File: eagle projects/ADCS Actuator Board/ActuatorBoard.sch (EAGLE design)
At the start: 142 parts, among them J19 TE_1-84953-1, J20 TE_1-84953-1, J21 TE_1-84953-1, U1 TVS991, U10 DRV10970_MOTOR_DRIVERDRV10970, U12 DRV10970_MOTOR_DRIVERDRV10970, U2 ADS7841E_2K5, U3 ADS7841E_2K5, U35 BD6210F-E2, U39 BD6210F-E2, U5 TVS991, U7 DRV10970_MOTOR_DRIVERDRV10970, U8 TVS991, U9 BD6210F-E2

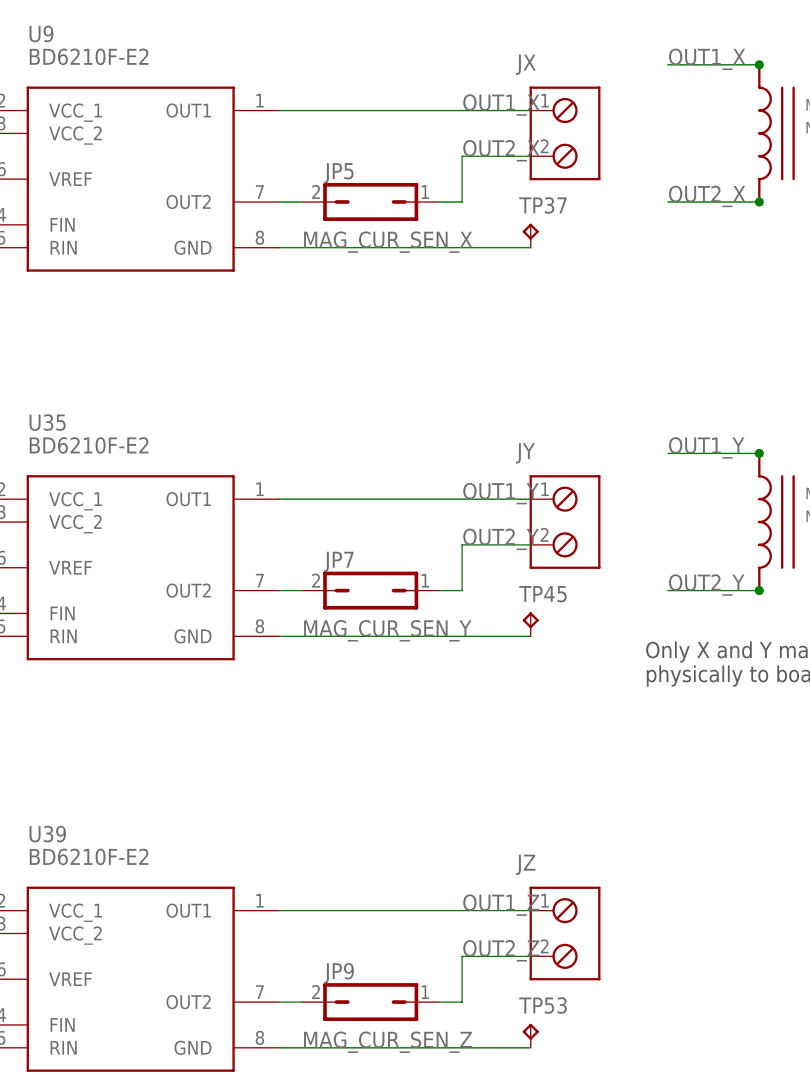
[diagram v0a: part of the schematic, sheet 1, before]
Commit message: Schematic Updates
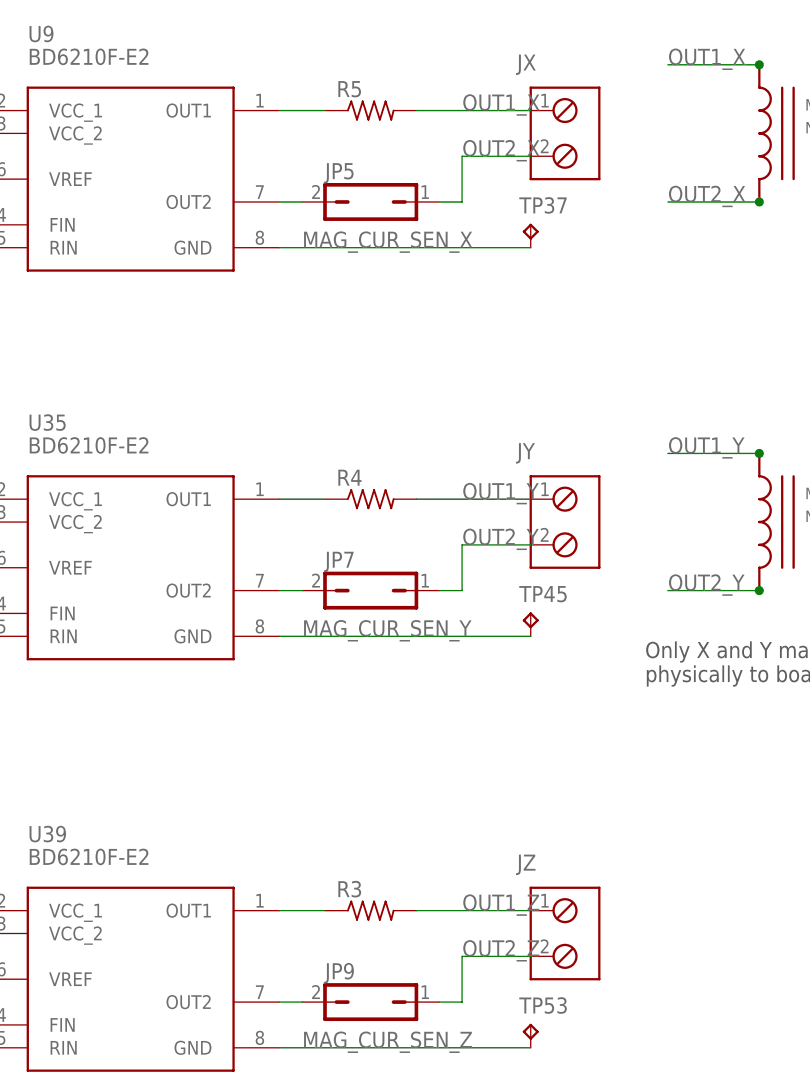
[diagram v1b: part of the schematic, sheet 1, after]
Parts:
- added R3, R4, R5: (no value), rcl:R-US_M0805
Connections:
- new net N$1: R3.1, U39.OUT1
- new net N$2: R4.1, U35.OUT1
- new net N$3: R5.1, U9.OUT1
- net OUT1_X: now also R5.2; no longer U9.OUT1
- net OUT1_Y: now also R4.2; no longer U35.OUT1
- net OUT1_Z: now also R3.2; no longer U39.OUT1
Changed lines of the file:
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@@
 <part name="R12" library="rcl" library_urn="urn:adsk.eagle:library:334" deviceset="R-US_" device="R0402" package3d_urn="urn:adsk.eagle:package:23547/3" value="4.7k"/>
 <part name="R15" library="rcl" library_urn="urn:adsk.eagle:library:334" deviceset="R-US_" device="R0402" package3d_urn="urn:adsk.eagle:package:23547/3" value="4.7k"/>
+<part name="R3" library="rcl" library_urn="urn:adsk.eagle:library:334" deviceset="R-US_" device="M0805" package3d_urn="urn:adsk.eagle:package:23556/2"/>
+<part name="R4" library="rcl" library_urn="urn:adsk.eagle:library:334" deviceset="R-US_" device="M0805" package3d_urn="urn:adsk.eagle:package:23556/2"/>
+<part name="R5" library="rcl" library_urn="urn:adsk.eagle:library:334" deviceset="R-US_" device="M0805" package3d_urn="urn:adsk.eagle:package:23556/2"/>
 </parts>
 <sheets>
@@
 <attribute name="VALUE" x="227.33" y="148.59" size="1.27" layer="96"/>
 </instance>
+<instance part="R3" gate="G$1" x="96.52" y="106.68" smashed="yes">
+<attribute name="NAME" x="92.71" y="108.1786" size="1.778" layer="95"/>
+<attribute name="VALUE" x="92.71" y="103.378" size="1.778" layer="96"/>
+</instance>
+<instance part="R4" gate="G$1" x="96.52" y="152.4" smashed="yes">
+<attribute name="NAME" x="92.71" y="153.8986" size="1.778" layer="95"/>
+<attribute name="VALUE" x="92.71" y="149.098" size="1.778" layer="96"/>
+</instance>
+<instance part="R5" gate="G$1" x="96.52" y="195.58" smashed="yes">
+<attribute name="NAME" x="92.71" y="197.0786" size="1.778" layer="95"/>
+<attribute name="VALUE" x="92.71" y="192.278" size="1.778" layer="96"/>
+</instance>
 </instances>
 <busses>
@@
 </segment>
 <segment>
-<pinref part="U9" gate="G$1" pin="OUT1"/>
 <pinref part="JX" gate="G$1" pin="1"/>
-<wire x1="114.3" y1="195.58" x2="86.36" y2="195.58" width="0.1524" layer="91"/>
 <label x="106.68" y="195.58" size="1.778" layer="95"/>
+<wire x1="114.3" y1="195.58" x2="101.6" y2="195.58" width="0.1524" layer="91"/>
+<pinref part="R5" gate="G$1" pin="2"/>
 </segment>
 </net>
@@
 </segment>
 <segment>
-<pinref part="U35" gate="G$1" pin="OUT1"/>
 <pinref part="JY" gate="G$1" pin="1"/>
-<wire x1="114.3" y1="152.4" x2="86.36" y2="152.4" width="0.1524" layer="91"/>
 <label x="106.68" y="152.4" size="1.778" layer="95"/>
+<wire x1="114.3" y1="152.4" x2="101.6" y2="152.4" width="0.1524" layer="91"/>
+<pinref part="R4" gate="G$1" pin="2"/>
 </segment>
 </net>
 <net name="OUT1_Z" class="0">
 <segment>
-<pinref part="U39" gate="G$1" pin="OUT1"/>
 <pinref part="JZ" gate="G$1" pin="1"/>
-<wire x1="114.3" y1="106.68" x2="86.36" y2="106.68" width="0.1524" layer="91"/>
 <label x="106.68" y="106.68" size="1.778" layer="95"/>
+<wire x1="114.3" y1="106.68" x2="101.6" y2="106.68" width="0.1524" layer="91"/>
+<pinref part="R3" gate="G$1" pin="2"/>
 </segment>
 </net>
@@
 <pinref part="U35" gate="G$1" pin="GND"/>
 <label x="88.9" y="137.16" size="1.778" layer="95"/>
+</segment>
+</net>
+<net name="N$1" class="0">
+<segment>
+<pinref part="U39" gate="G$1" pin="OUT1"/>
+<wire x1="91.44" y1="106.68" x2="86.36" y2="106.68" width="0.1524" layer="91"/>
+<pinref part="R3" gate="G$1" pin="1"/>
+</segment>
+</net>
+<net name="N$2" class="0">
+<segment>
+<pinref part="U35" gate="G$1" pin="OUT1"/>
+<wire x1="91.44" y1="152.4" x2="86.36" y2="152.4" width="0.1524" layer="91"/>
+<pinref part="R4" gate="G$1" pin="1"/>
+</segment>
+</net>
+<net name="N$3" class="0">
+<segment>
+<pinref part="U9" gate="G$1" pin="OUT1"/>
+<wire x1="91.44" y1="195.58" x2="86.36" y2="195.58" width="0.1524" layer="91"/>
+<pinref part="R5" gate="G$1" pin="1"/>
 </segment>
 </net>
@@
 <text x="111.76" y="53.34" size="1.778" layer="97">NC</text>
 <text x="261.62" y="7.62" size="2.54" layer="94">A</text>
-<text x="182.88" y="53.34" size="1.778" layer="97">Hall sensors on Maxon motor require external pull-up resistor</text>
+<text x="175.26" y="208.28" size="1.778" layer="97">Hall sensors on Maxon motor require external pull-up resistor</text>
 <text x="68.58" y="200.66" size="1.778" layer="97">Only Z-axis Reaction wheel mounted physically to PCB</text>
 </plain>

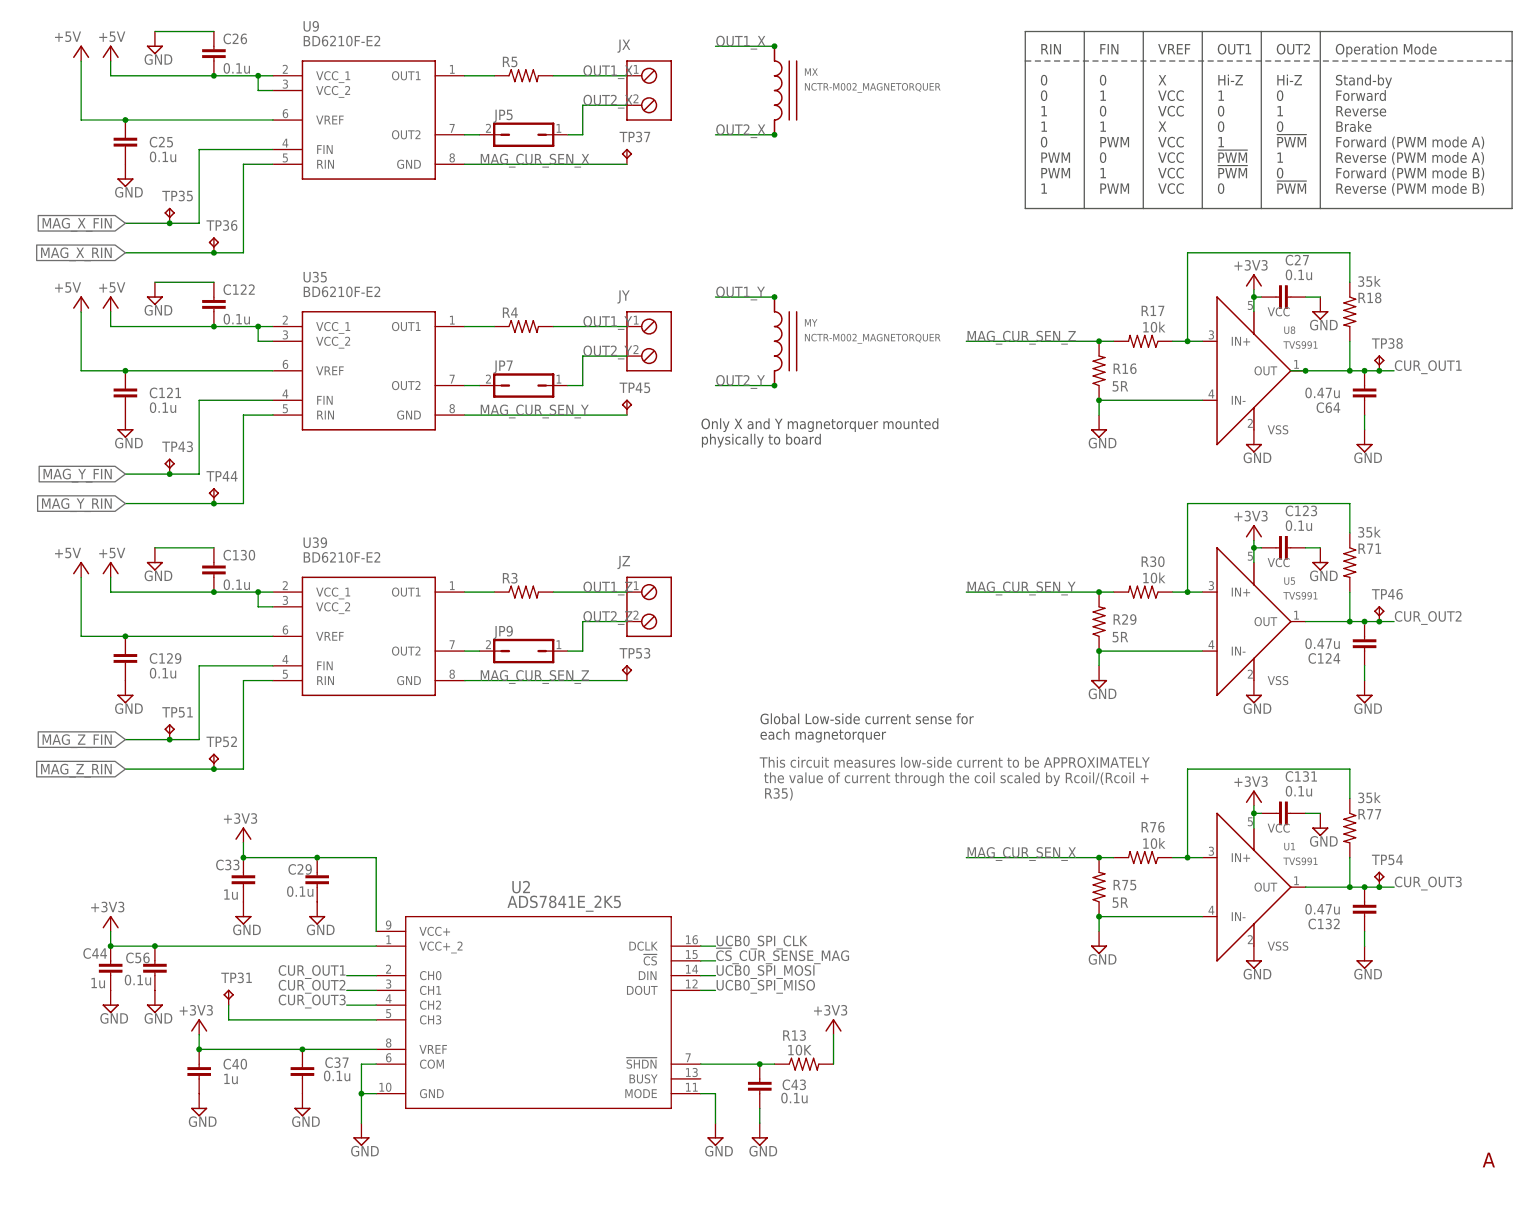
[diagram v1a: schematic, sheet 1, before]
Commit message: Updated current sense circuitry
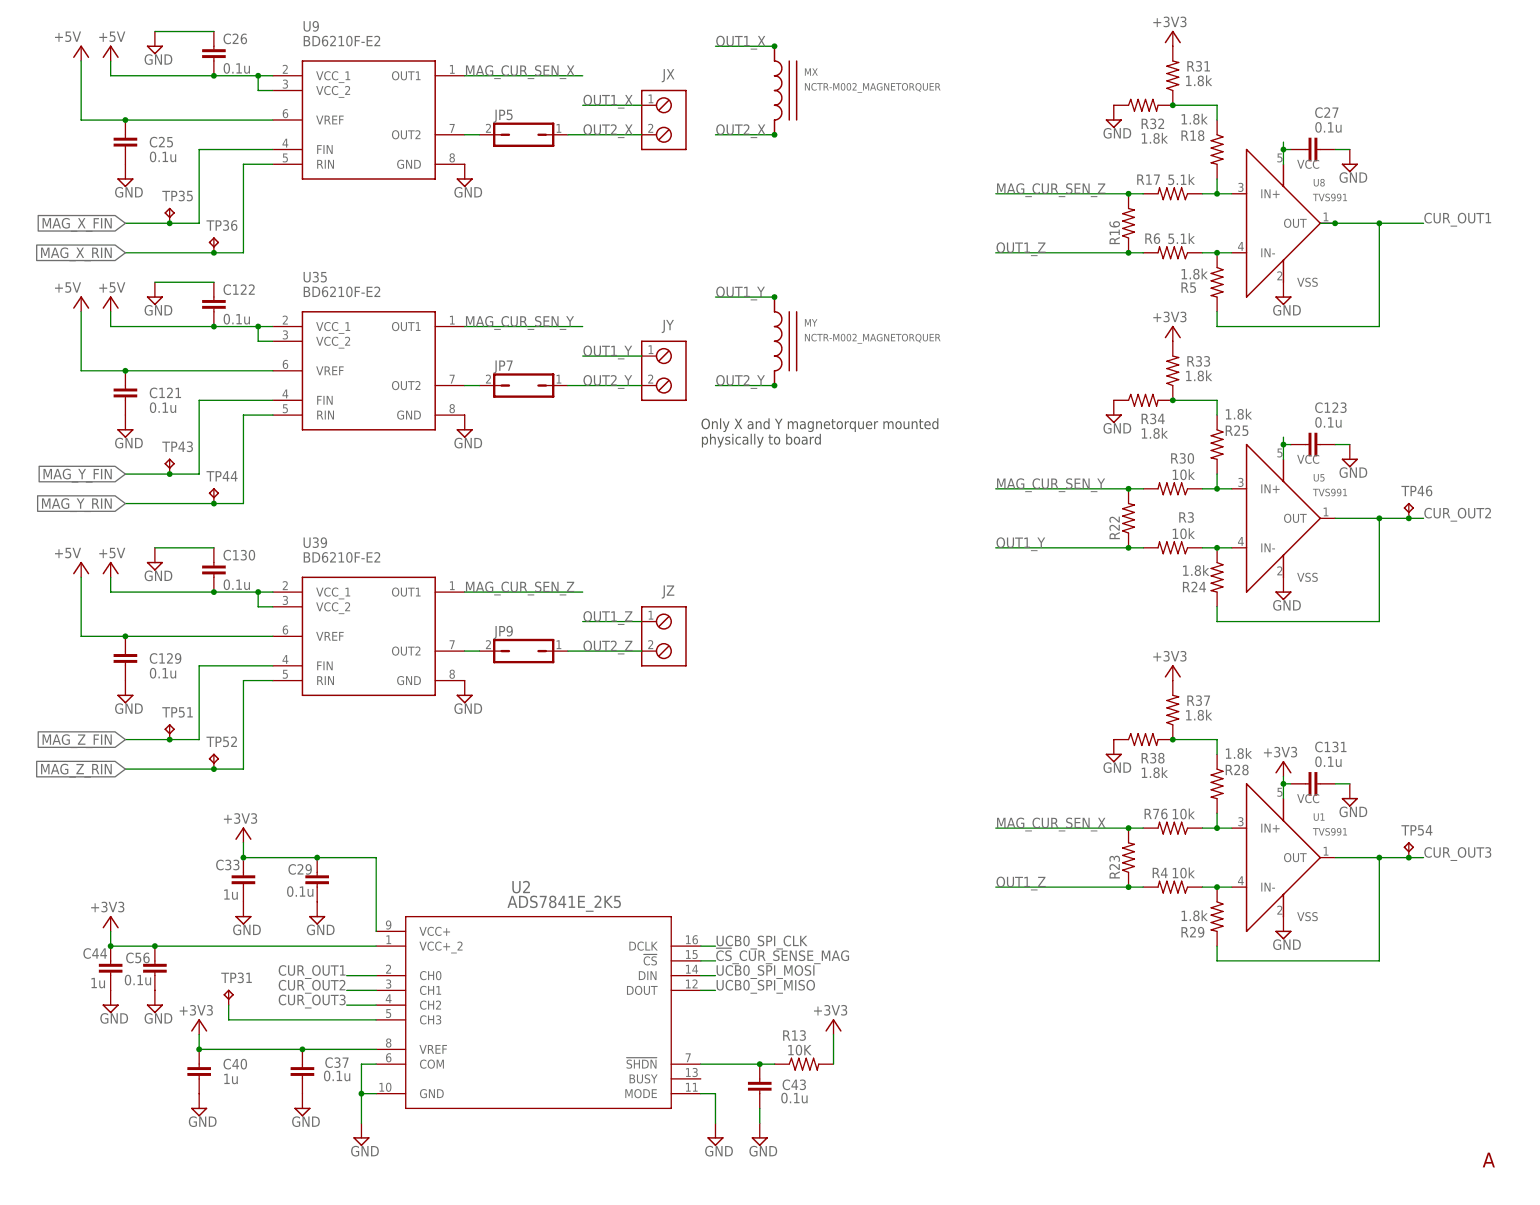
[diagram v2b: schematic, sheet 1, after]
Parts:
- removed C124, C132, C64: 0.47u, rcl:C-EUC0603
- removed R71, R77: 35k, rcl:R-US_R0402
- removed R75: 5R, rcl:R-US_R0402
- removed TP37, TP38, TP45, TP53: TESTPOINT, my_library:TESTPOINT
- added R22, R23: (no value), rcl:R-US_M0805
- added R24, R25, R28, R31, R32, R33, R34, R37, R38: 1.8k, rcl:R-US_R0402
- added R6: 5.1k, rcl:R-US_R0402
- R16: value 5R -> (none); device rcl:R-US_R0402 -> rcl:R-US_M0805
- R17: value 10k -> 5.1k
- R18: value 35k -> 1.8k
- R29: value 5R -> 1.8k
- R3, R4: value (none) -> 10k; device rcl:R-US_M0805 -> rcl:R-US_R0402
- R5: value (none) -> 1.8k; device rcl:R-US_M0805 -> rcl:R-US_R0402
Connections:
- removed net N$3: R5.1, U9.OUT1
- removed net N$68: R76.1, R77.1, U1.IN+
- new net N$10: R28.2, R76.1, U1.IN+
- new net N$17: R33.1, R34.2
- new net N$18: R28.1, R37.1, R38.2
- new net N$4: R5.1, R6.1, U8.IN-
- new net N$6: R24.1, R3.1, U5.IN-
- new net N$7: R29.1, R4.1, U1.IN-
- new net N$8: R17.1, R18.2, U8.IN+
- new net N$9: R25.2, R30.1, U5.IN+
- net +3V3: now also R31.2, R33.2, R37.2; no longer C123.1, C27.1, U5.VCC, U8.VCC
- net CUR_OUT1: now also R5.2; no longer C64.2, R18.2, TP38.TP
- net CUR_OUT2: now also R24.2; no longer C124.2, R71.2
- net CUR_OUT3: now also R29.2; no longer C132.2, R77.2
- net GND: now also R32.1, R34.1, R38.1, U35.GND, U39.GND, U9.GND; no longer C124.1, C132.1, C64.1, R16.1, R29.1, R75.1, U1.IN-, U5.IN-, U8.IN-
- net MAG_CUR_SEN_X: now also R23.2, U9.OUT1; no longer R75.2, TP37.TP, U9.GND
- net MAG_CUR_SEN_Y: now also R22.2, U35.OUT1; no longer R29.2, TP45.TP, U35.GND
- net MAG_CUR_SEN_Z: now also U39.OUT1; no longer TP53.TP, U39.GND
- net N$1: now also C123.1, U5.VCC; no longer R3.1, U39.OUT1
- net N$2: now also C27.1, U8.VCC; no longer R4.1, U35.OUT1
- net N$21: now also R31.1, R32.2; no longer R17.1, U8.IN+
- net N$48: now also R25.1; no longer R30.1, R71.1, U5.IN+
- net OUT1_X: no longer R5.2
- net OUT1_Y: now also R22.1, R3.2; no longer R4.2
- net OUT1_Z: now also R16.1, R23.1, R4.2, R6.2; no longer R3.2
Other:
- note removed: "Global Low-side current sense for each magnetorquer"
- note removed: "This circuit measures low-side current to be APPROXIMATELY the value of current through the coil scaled by Rcoil/(Rcoil + R35)"
- moved on the sheet: C123, C131, C27, JX, JY, JZ, R16, R17, R18, R29, R3, R30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
